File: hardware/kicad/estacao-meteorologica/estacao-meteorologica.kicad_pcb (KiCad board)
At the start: 2 copper layers, 109.4 x 61.3 mm, 126 parts, among them J101 Header, 1x02, P2.54 mm, J102 Header, 1x06, P2.54 mm, J103 Header, 1x03, P2.54 mm, J221 JST-XH, 1x04, P2.50 mm, J301 RJ11 6P6C, 90°, J501 RJ11 6P6C, 90°, J601 DC jack, 2.0 mm, J602 JST-XH, 1x02, P2.50 mm, J701 U.FL, 50 Ω, J801 microSD socket, TF-15x15, Q601 DMP6023LE-13, SW101 Tactile switch, SPST, U101 STM32F446RET6, U211 BMP280, U231 DHT22, U301 SN74LVC1G17DBVR, U401 SN74LVC1G17DBVR, U601 AP63205WU-7, U602 TLV62569DBVR, U701 LORA1276-C1-915MHZ, U801 SN74LVC125APWR, U802 EMIF06-MSD02N16, Y101 32.768 kHz, CL 7 pF, Y102 8 MHz, CL 10 pF

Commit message: Add test points necessarios para debug
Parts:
- added TP211: I2C1_SCL, TestPoint:TestPoint_Pad_D1.0mm, F.Cu at (126.2, 65.6)
- added TP212: I2C1_SDA, TestPoint:TestPoint_Pad_D1.0mm, F.Cu at (123.4, 65.4)
- added TP213: GND, TestPoint:TestPoint_Pad_D1.0mm, F.Cu at (127.5, 58.5)
- added TP221: BH_I2C3_SCL, TestPoint:TestPoint_Pad_D1.0mm, F.Cu at (115.9, 64.1)
- added TP222: BH_I2C3_SDA, TestPoint:TestPoint_Pad_D1.0mm, F.Cu at (118.7, 63.7)
- added TP223: GND, TestPoint:TestPoint_Pad_D1.0mm, F.Cu at (116.6, 60.0)
- added TP231: DHT22_DATA, TestPoint:TestPoint_Pad_D1.0mm, F.Cu at (126.4, 98.5)
- added TP232: GND, TestPoint:TestPoint_Pad_D1.0mm, F.Cu at (131.4, 107.1)
- TP301, TP302, TP303, TP401, TP402, TP403, TP501, TP502, TP503: footprint TestPoint:TestPoint_Pad_D1.5mm -> TestPoint:TestPoint_Pad_D1.0mm
- moved H902 69.9 mm to (137.0, 96.0)

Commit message: Refact: tirei estagio de 12V -> 5V e agora é direto 12V -> 3V
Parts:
- L601: value 4.7 µH -> 3.9 µH; footprint Inductor_SMD:L_Sunlord_MWSA0603S -> Inductor_SMD:L_APV_ANR5040
- U601: value AP63205WU-7 -> AP63203WU-7
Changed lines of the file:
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@@
 	(generator_version "9.0")
 	(general
-		(thickness 1.6)
+		(thickness 1.69)
 		(legacy_teardrops no)
 	)
@@
 	(layers
 		(0 "F.Cu" signal)
-		(2 "B.Cu" signal)
+		(2 "B.Cu" power)
 		(9 "F.Adhes" user "F.Adhesive")
 		(11 "B.Adhes" user "B.Adhesive")
@@
 	)
 	(setup
+		(stackup
+			(layer "F.SilkS"
+				(type "Top Silk Screen")
+			)
+			(layer "F.Paste"
+				(type "Top Solder Paste")
+			)
+			(layer "F.Mask"
+				(type "Top Solder Mask")
+				(thickness 0.01)
+			)
+			(layer "F.Cu"
+				(type "copper")
+				(thickness 0.035)
+			)
+			(layer "dielectric 1"
+				(type "core")
+				(thickness 1.6)
+				(material "FR4")
+				(epsilon_r 4.5)
+				(loss_tangent 0.02)
+			)
+			(layer "B.Cu"
+				(type "copper")
+				(thickness 0.035)
+			)
+			(layer "B.Mask"
+				(type "Bottom Solder Mask")
+				(thickness 0.01)
+			)
+			(layer "B.Paste"
+				(type "Bottom Solder Paste")
+			)
+			(layer "B.SilkS"
+				(type "Bottom Silk Screen")
+			)
+			(copper_finish "None")
+			(dielectric_constraints no)
+		)
 		(pad_to_mask_clearance 0)
 		(allow_soldermask_bridges_in_footprints no)
@@
 			)
 		)
-		(property "Value" "AP63205WU-7"
+		(property "Value" "AP63203WU-7"
 			(at 0 2.4 0)
 			(layer "F.Fab")
@@
 			)
 		)
-		(property "Datasheet" "https://www.lcsc.com/datasheet/lcsc_datasheet_2210280930_Diodes-Incorporated-AP63205WU-7_C2071056.pdf"
+		(property "Datasheet" "https://www.diodes.com/datasheet/download/AP63200-AP63201-AP63203-AP63205.pdf"
 			(at 0 0 0)
 			(layer "F.Fab")
@@
 			)
 		)
-		(property "Description" "-40℃~+85℃@(TA) 1 1.1MHz 22uA 2A 3.8V~32V 5V Buck Built-in Fixed Overcurrent Protection、Light load efficient mode、Cycle-by-cycle current limiting、Hiccup current limiting、EMI optimization (spread spectrum) Step-down type Yes TSOT-23-6 DC-DC Converters RoHS"
+		(property "Description" "Buck sincrono fixo 3,3V; VIN 3,8-32V; 2A; 1,1MHz; TSOT-23-6; protecao contra sobrecorrente e spread-spectrum EMI; RoHS"
 			(at 0 0 0)
 			(layer "F.Fab")
@@
 			)
 		)
-		(property "MPN" "AP63205WU-7"
+		(property "MPN" "AP63203WU-7"
 			(at 0 0 0)
 			(unlocked yes)
@@
 			)
 		)
-		(property "LCSC" "C2071056"
+		(property "LCSC" "C780769"
 			(at 0 0 0)
 			(unlocked yes)
@@
 			)
 		)
-		(property "LCSC Part" "C2071056"
+		(property "LCSC Part" "C780769"
 			(at 0 0 0)
 			(unlocked yes)
@@
 			)
 		)
-		(property "Rating" "5V fixos; 2A CI; VIN3.8-32V; 1.1MHz; IQtip22uA"
+		(property "Rating" "3,3V fixos; 2A CI; VIN3,8-32V; 1,1MHz; IQ tipico 22uA"
 			(at 0 0 0)
 			(unlocked yes)
@@
 			)
 		)
-		(property "Function" "Converte VIN_MAIN para5V; EN ligado aVIN; FB direto na saida filtrada"
+		(property "Function" "Converte VIN_MAIN diretamente para +3V3; EN ligado a VIN; FB direto na saida filtrada"
 			(at 0 0 0)
 			(unlocked yes)
@@
 			)
 		)
-		(property "Status_Ficha" "Conferido no catalogo em 2026-09-24; verificar estoque ao comprar"
+		(property "Status_Ficha" "Ficha do fabricante e catalogo LCSC conferidos em 2026-09-27; verificar estoque ao comprar"
 			(at 0 0 0)
 			(unlocked yes)
@@
 			)
 		)
-		(property "Specification" "5V fixos; 2A CI; VIN3.8-32V; 1.1MHz; IQtip22uA"
+		(property "Specification" "3,3V fixos; 2A CI; VIN3,8-32V; 1,1MHz; IQ tipico 22uA"
 			(at 0 0 0)
 			(unlocked yes)
@@
 			)
 		)
-		(property "Verification" "Conferido no catalogo em 2026-09-24; verificar estoque ao comprar"
+		(property "Verification" "Ficha do fabricante e catalogo LCSC conferidos em 2026-09-27; verificar estoque ao comprar"
 			(at 0 0 0)
 			(unlocked yes)
@@
 		)
 	)
-	(footprint "Inductor_SMD:L_Sunlord_MWSA0603S"
+	(footprint "Inductor_SMD:L_APV_ANR5040"
 		(layer "F.Cu")
 		(at 80.1 72.3)
-		(descr "Inductor, Sunlord, MWSA0603S, 7.0x6.6x2.8mm, (https://sunlordinc.com/Download.aspx?file=L1VwbG9hZEZpbGVzL1BERl9DYXQvMjAyMjExMTUxNDQ4MDU0NTQucGRm&lan=en), generated with kicad-footprint-generator gen_inductor.py")
-		(tags "mwsa")
+		(descr "Inductor, APV, ANR5040, 5.0x5.0x4.0mm, (http://en.apvind.com/public/upload/20240407/3375c395e460caa8519b4d637d9113ce.pdf), generated with kicad-footprint-generator gen_inductor.py")
+		(tags "wirewound power shielded")
 		(property "Reference" "L601"
-			(at 0 -4.25 0)
+			(at 0 -3.45 0)
 			(layer "F.SilkS")
 			(effects
@@
 			)
 		)
-		(property "Value" "4.7 µH"
-			(at 0 4.25 0)
+		(property "Value" "3.9 µH"
+			(at 0 3.45 0)
 			(layer "F.Fab")
 			(effects
@@
 			)
 		)
-		(property "Datasheet" "https://www.lcsc.com/datasheet/lcsc_datasheet_2310251550_Sunlord-MWSA0603S-4R7MT_C408447.pdf"
+		(property "Datasheet" "https://www.lcsc.com/product-detail/Power-Inductors_APV-ANR5040T3R9M_C7427132.html"
 			(at 0 0 0)
 			(layer "F.Fab")
@@
 			)
 		)
-		(property "Description" "33mΩ 4.7uH 6A 9A ±20% SMD,7x6.6mm Power Inductors RoHS"
+		(property "Description" "Indutor de potencia blindado 3,9uH ±20%; Irms 3,7A; Isat 4,2A; SMD 5x5mm; RoHS"
 			(at 0 0 0)
 			(layer "F.Fab")
@@
 			)
 		)
-		(property "Manufacturer" "Sunlord"
+		(property "Manufacturer" "APV"
 			(at 0 0 0)
 			(unlocked yes)
@@
 			)
 		)
-		(property "MPN" "MWSA0603S-4R7MT"
+		(property "MPN" "ANR5040T3R9M"
 			(at 0 0 0)
 			(unlocked yes)
@@
 			)
 		)
-		(property "LCSC" "C408447"
+		(property "LCSC" "C7427132"
 			(at 0 0 0)
 			(unlocked yes)
@@
 			)
 		)
-		(property "LCSC Part" "C408447"
+		(property "LCSC Part" "C7427132"
 			(at 0 0 0)
 			(unlocked yes)
@@
 			)
 		)
-		(property "Rating" "Isat min7.2A/tip9A; Irms min5A; DCRmax33mOhm"
+		(property "Rating" "L=3,9uH ±20%; Irms 3,7A; Isat 4,2A; indutor blindado; corpo 5x5x4mm"
 			(at 0 0 0)
 			(unlocked yes)
@@
 			)
 		)
-		(property "Modelo 3D" "${KICAD9_3DMODEL_DIR}/Inductor_SMD.3dshapes/L_Sunlord_MWSA0603S.step"
+		(property "Modelo 3D" "${KICAD9_3DMODEL_DIR}/Inductor_SMD.3dshapes/L_APV_ANR5040.step"
 			(at 0 0 0)
 			(unlocked yes)
@@
 			)
 		)
-		(property "Status_Ficha" "Conferido no catalogo em 2026-09-24; verificar estoque ao comprar"
+		(property "Status_Ficha" "Ficha do fabricante e catalogo LCSC conferidos em 2026-09-27; verificar estoque ao comprar"
 			(at 0 0 0)
 			(unlocked yes)
@@
 			)
 		)
-		(property "Specification" "Isat min7.2A/tip9A; Irms min5A; DCRmax33mOhm"
+		(property "Specification" "L=3,9uH ±20%; Irms 3,7A; Isat 4,2A; indutor blindado; corpo 5x5x4mm"
 			(at 0 0 0)
 			(unlocked yes)
@@
 			)
 		)
-		(property "Verification" "Conferido no catalogo em 2026-09-24; verificar estoque ao comprar"
+		(property "Verification" "Ficha do fabricante e catalogo LCSC conferidos em 2026-09-27; verificar estoque ao comprar"
 			(at 0 0 0)
 			(unlocked yes)
@@
 		(attr smd)
 		(fp_line
-			(start -3.61 -3.41)
-			(end 3.61 -3.41)
+			(start -2.61 -2.61)
+			(end 2.61 -2.61)
 			(stroke
 				(width 0.12)
@@
 		)
 		(fp_line
-			(start -3.61 -2.01)
-			(end -3.61 -3.41)
+			(start -2.61 -2.36)
+			(end -2.61 -2.61)
 			(stroke
 				(width 0.12)
@@
 		)
 		(fp_line
-			(start -3.61 3.41)
-			(end -3.61 2.01)
+			(start -2.61 2.61)
+			(end -2.61 2.36)
 			(stroke
 				(width 0.12)
@@
 		)
 		(fp_line
-			(start 3.61 -3.41)
-			(end 3.61 -2.01)
+			(start 2.61 -2.61)
+			(end 2.61 -2.36)
 			(stroke
 				(width 0.12)
@@
 		)
 		(fp_line
-			(start 3.61 2.01)
-			(end 3.61 3.41)
+			(start 2.61 2.36)
+			(end 2.61 2.61)
 			(stroke
 				(width 0.12)
@@
 		)
 		(fp_line
-			(start 3.61 3.41)
-			(end -3.61 3.41)
+			(start 2.61 2.61)
+			(end -2.61 2.61)
 			(stroke
 				(width 0.12)
@@
 		)
 		(fp_line
-			(start -4.45 -2)
-			(end -3.75 -2)
+			(start -2.8 -2.35)
+			(end -2.75 -2.35)
 			(stroke
 				(width 0.05)
@@
 		)
 		(fp_line
-			(start -4.45 2)
-			(end -4.45 -2)
+			(start -2.8 2.35)
+			(end -2.8 -2.35)
 			(stroke
 				(width 0.05)
@@
 		)
 		(fp_line
-			(start -3.75 -3.55)
-			(end 3.75 -3.55)
+			(start -2.75 -2.75)
+			(end 2.75 -2.75)
 			(stroke
 				(width 0.05)
@@
 		)
 		(fp_line
-			(start -3.75 -2)
-			(end -3.75 -3.55)
+			(start -2.75 -2.35)
+			(end -2.75 -2.75)
 			(stroke
 				(width 0.05)
@@
 		)
 		(fp_line
-			(start -3.75 2)
-			(end -4.45 2)
+			(start -2.75 2.35)
+			(end -2.8 2.35)
 			(stroke
 				(width 0.05)
@@
 		)
 		(fp_line
-			(start -3.75 3.55)
-			(end -3.75 2)
+			(start -2.75 2.75)
+			(end -2.75 2.35)
 			(stroke
 				(width 0.05)
@@
 		)
 		(fp_line
-			(start 3.75 -3.55)
-			(end 3.75 -2)
+			(start 2.75 -2.75)
+			(end 2.75 -2.35)
 			(stroke
 				(width 0.05)
@@
 		)
 		(fp_line
-			(start 3.75 -2)
-			(end 4.45 -2)
+			(start 2.75 -2.35)
+			(end 2.8 -2.35)
 			(stroke
 				(width 0.05)
@@
 		)
 		(fp_line
-			(start 3.75 2)
-			(end 3.75 3.55)
+			(start 2.75 2.35)
+			(end 2.75 2.75)
 			(stroke
 				(width 0.05)
@@
 		)
 		(fp_line
-			(start 3.75 3.55)
-			(end -3.75 3.55)
+			(start 2.75 2.75)
+			(end -2.75 2.75)
 			(stroke
 				(width 0.05)
@@
 		)
 		(fp_line
-			(start 4.45 -2)
-			(end 4.45 2)
+			(start 2.8 -2.35)
+			(end 2.8 2.35)
 			(stroke
 				(width 0.05)
@@
 		)
 		(fp_line
-			(start 4.45 2)
-			(end 3.75 2)
+			(start 2.8 2.35)
+			(end 2.75 2.35)
 			(stroke
 				(width 0.05)
@@
 		)
 		(fp_rect
-			(start -3.5 -3.3)
-			(end 3.5 3.3)
+			(start -2.5 -2.5)
+			(end 2.5 2.5)
 			(stroke
 				(width 0.1)
@@
 		)
 		(pad "1" smd roundrect
-			(at -3.025 0)
-			(size 2.35 3.5)
+			(at -1.85 0)
+			(size 1.4 4.2)
 			(layers "F.Cu" "F.Mask" "F.Paste")
-			(roundrect_rratio 0.106383)
+			(roundrect_rratio 0.178571)
 			(net 7 "Net-(U601-SW)")
 			(pinfunction "1")
@@
 		)
 		(pad "2" smd roundrect
-			(at 3.025 0)
-			(size 2.35 3.5)
+			(at 1.85 0)
+			(size 1.4 4.2)
 			(layers "F.Cu" "F.Mask" "F.Paste")
-			(roundrect_rratio 0.106383)
+			(roundrect_rratio 0.178571)
 			(net 9 "+5V")
 			(pinfunction "2")
@@
 		)
 		(embedded_fonts no)
-		(model "${KICAD9_3DMODEL_DIR}/Inductor_SMD.3dshapes/L_Sunlord_MWSA0603S.step"
+		(model "${KICAD9_3DMODEL_DIR}/Inductor_SMD.3dshapes/L_APV_ANR5040.step"
 			(offset
 				(xyz 0 0 0)

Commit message: rotemento 3.0
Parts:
- removed C608: 4.7 µF, 25 V, Capacitor_SMD:C_0805_2012Metric
- removed C609, C610, C611: 10 µF, 6.3 V, Capacitor_SMD:C_0402_1005Metric
- removed L602: 2.2 µH, Hardware_Power:L_Abracon_ASPI-0530HI
- removed R602: 453 kΩ, 1 %, Resistor_SMD:R_0603_1608Metric
- removed R603: 100 kΩ, 1 %, Resistor_SMD:R_0402_1005Metric
- removed TP602: +5V, TestPoint:TestPoint_Pad_D1.5mm
- removed U602: TLV62569DBVR, Package_TO_SOT_SMD:SOT-23-5
- J801: footprint Hardware_SD_Interface:microSD_SOFNG_TF-15x15 -> Hardware_SD_Interface:microSD_SOFNG_TF-15x15_C111196
- moved H902 97.0 mm to (43.1, 120.3)
- moved C105 33.3 mm to (118.6, 89.3)
- moved D221 29.7 mm to (139.1, 63.2)
- moved D222 29.7 mm to (142.8, 63.2)
- moved J221 29.7 mm to (133.3, 58.6)
- moved TP222 26.5 mm to (145.2, 63.2)
- moved TP604 16.6 mm to (75.9, 81.8)
- moved C113 16.0 mm to (102.5, 87.7), turned to -90 degrees
- moved TP603 15.1 mm to (85.4, 72.0)
- moved TP601 14.4 mm to (70.8, 70.5)
- moved TP223 12.1 mm to (128.4, 57.4)
- moved TP213 9.91 mm to (122.4, 67.0)
- moved TP211 6.90 mm to (119.3, 65.8)
- moved TP212 5.66 mm to (118.1, 63.4)
- moved J101 5.14 mm to (106.4, 65.2), turned to 90 degrees
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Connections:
- net BH_I2C3_SCL renamed /BH1750_INTERFACE/BH_I2C3_SCL
- net Net-(U601-SW) renamed /ALIMENTAÇÃO/V_SW
- C606 pad 1: +5V -> +3V3
- C607 pad 1: +5V -> +3V3
- D222 pad 2: BH_I2C3_SDA -> /BH1750_INTERFACE/BH_I2C3_SDA
- J221 pad 2: +3V3 -> /BH1750_INTERFACE/BH_I2C3_SDA
- J221 pad 4: BH_I2C3_SDA -> unconnected-(J221-Pin_4-Pad4)
- L601 pad 2: +5V -> +3V3
- R106 pad 2: BH_I2C3_SDA -> /BH1750_INTERFACE/BH_I2C3_SDA
- TP222 pad 1: BH_I2C3_SDA -> /BH1750_INTERFACE/BH_I2C3_SDA
- U101 pad 40: BH_I2C3_SDA -> /BH1750_INTERFACE/BH_I2C3_SDA
- U601 pad 1: +5V -> +3V3
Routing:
- net +3V3: track 0.00 -> 143.6 mm, vias 0 -> 4
- net GND: track 0.00 -> 90.5 mm, vias 0 -> 43
- net /INTERFACES METEOROLÓGICAS/WIND_SPEED_PULSE: track 0.00 -> 63.5 mm, vias 0 -> 4
- net /INTERFACES METEOROLÓGICAS/WIND_DIR_ADC: track 0.00 -> 61.7 mm, vias 0 -> 2
- net /INTERFACES METEOROLÓGICAS/RAIN_PULSE: track 0.00 -> 45.7 mm
- net VBAT: track 0.00 -> 42.4 mm, vias 0 -> 2
- net /MCU E DEPURAÇÃO/DHT22_DATA: track 0.00 -> 38.7 mm, vias 0 -> 2
- net /RÁDIO LoRa/+3V3_LORA: track 0.00 -> 37.8 mm
- net /BH1750_INTERFACE/BH_I2C3_SCL: track 0.00 -> 33.5 mm
- net /ALIMENTAÇÃO/VIN_MAIN: track 0.00 -> 28.1 mm
- net /MCU E DEPURAÇÃO/LORA_SPI_SCK: track 0.00 -> 26.0 mm
- net /MCU E DEPURAÇÃO/LORA_DIO2: track 0.00 -> 19.4 mm, vias 0 -> 2
- net /MCU E DEPURAÇÃO/I2C1_SDA: track 0.00 -> 18.2 mm
- net Net-(D601-A2): track 0.00 -> 18.1 mm
- net /MCU E DEPURAÇÃO/LORA_SPI_MOSI: track 0.00 -> 17.6 mm
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- added copper zone on F.Cu, net +3V3
- added copper zone on F.Cu, net /ALIMENTAÇÃO/VIN_MAIN
- added copper zone on F.Cu, net /ALIMENTAÇÃO/V_SW
- added copper zone on B.Cu, net GND
- added copper zone on F.Cu, net GND

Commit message: feat(hardware): consolida revisão PCB V2
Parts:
- TP304, TP404, TP504, TP601, TP603, TP604: footprint TestPoint:TestPoint_Pad_D1.5mm -> TestPoint:TestPoint_Pad_D1.0mm
- moved J102 48.8 mm to (113.2, 57.8)
- moved BT101 37.1 mm to (83.6, 60.4), turned to 180 degrees
- moved SW101 28.1 mm to (108.3, 97.4), turned to 0 degrees
- moved C113 26.5 mm to (97.5, 61.7)
- moved TP213 26.3 mm to (97.5, 58.4)
- moved TP222 25.2 mm to (120.0, 63.5)
- moved R801 21.2 mm to (95.3, 93.0)
- moved U801 21.2 mm to (91.6, 90.4)
- moved C802 21.2 mm to (94.0, 95.5)
- moved D222 21.1 mm to (121.8, 62.2)
- moved C114 20.7 mm to (102.8, 97.4), turned to -90 degrees
- moved J801 19.6 mm to (79.1, 95.9)
- moved R102 18.8 mm to (101.0, 97.4)
- moved R802 18.2 mm to (71.9, 88.8)
- moved C801 18.1 mm to (68.7, 93.7)
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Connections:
- D221 pad 2: /BH1750_INTERFACE/BH_I2C3_SCL -> /BH1750_INTERFACE/BH_I2C3_SDA
- D222 pad 2: /BH1750_INTERFACE/BH_I2C3_SDA -> /BH1750_INTERFACE/BH_I2C3_SCL
- J102 pad 2: GND -> SWDIO
- J102 pad 3: SWDIO -> SWCLK
- J102 pad 4: SWCLK -> SWO
- J102 pad 6: SWO -> GND
- J221 pad 2: /BH1750_INTERFACE/BH_I2C3_SDA -> /BH1750_INTERFACE/BH_I2C3_SCL
- J221 pad 3: /BH1750_INTERFACE/BH_I2C3_SCL -> /BH1750_INTERFACE/BH_I2C3_SDA
- J221 pad 4: unconnected-(J221-Pin_4-Pad4) -> +3V3
- R801 pad 1: /CARTÃO microSD/SD_SPI_CS -> /CARTÃO microSD/SD_SPI_MOSI
- TP221 pad 1: /BH1750_INTERFACE/BH_I2C3_SCL -> /BH1750_INTERFACE/BH_I2C3_SDA
- TP222 pad 1: /BH1750_INTERFACE/BH_I2C3_SDA -> /BH1750_INTERFACE/BH_I2C3_SCL
- U801 pad 11: SD_CS_BUF -> SD_MOSI_BUF
- U801 pad 12: /CARTÃO microSD/SD_SPI_CS -> /CARTÃO microSD/SD_SPI_MOSI
- U801 pad 2: /CARTÃO microSD/SD_SPI_MOSI -> SD_MISO_BUF
- U801 pad 3: SD_MOSI_BUF -> /CARTÃO microSD/SD_MISO
- U801 pad 5: SD_MISO_BUF -> /CARTÃO microSD/SD_SCK
- U801 pad 6: /CARTÃO microSD/SD_MISO -> SD_SCK_BUF
- U801 pad 8: SD_SCK_BUF -> SD_CS_BUF
- U801 pad 9: /CARTÃO microSD/SD_SCK -> /CARTÃO microSD/SD_SPI_CS
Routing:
- net +3V3: track 143.6 -> 404.9 mm, vias 4 -> 5
- net AVREF_SENSOR: track 6.06 -> 53.3 mm, vias 0 -> 2
- net NRST: track 11.4 -> 56.1 mm, vias 0 -> 3
- net GND: track 90.5 -> 121.3 mm, vias 43 -> 95
- net /MCU E DEPURAÇÃO/LORA_RST: track 16.1 -> 42.4 mm, vias 0 -> 2
- net SWDIO: track 0.00 -> 23.9 mm, vias 0 -> 1
- net VBAT: track 42.4 -> 20.8 mm
- net /BH1750_INTERFACE/BH_I2C3_SDA: track 17.0 -> 37.9 mm, vias 0 -> 4
- net /CARTÃO microSD/SD_SPI_CS: track 0.00 -> 20.7 mm
- net /MCU E DEPURAÇÃO/LORA_NSS: track 12.0 -> 31.9 mm, vias 0 -> 2
- net SWO: track 0.00 -> 19.2 mm, vias 0 -> 1
- net SWCLK: track 0.00 -> 19.0 mm, vias 0 -> 1
- net /CARTÃO microSD/SD_SPI_MOSI: track 0.00 -> 14.6 mm
- net /CARTÃO microSD/SD_SCK: track 0.00 -> 14.1 mm
- net SD_CARD_DAT1: track 0.00 -> 13.8 mm
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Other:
- board size 109.4 x 61.3 mm -> 96.9 x 56.3 mm

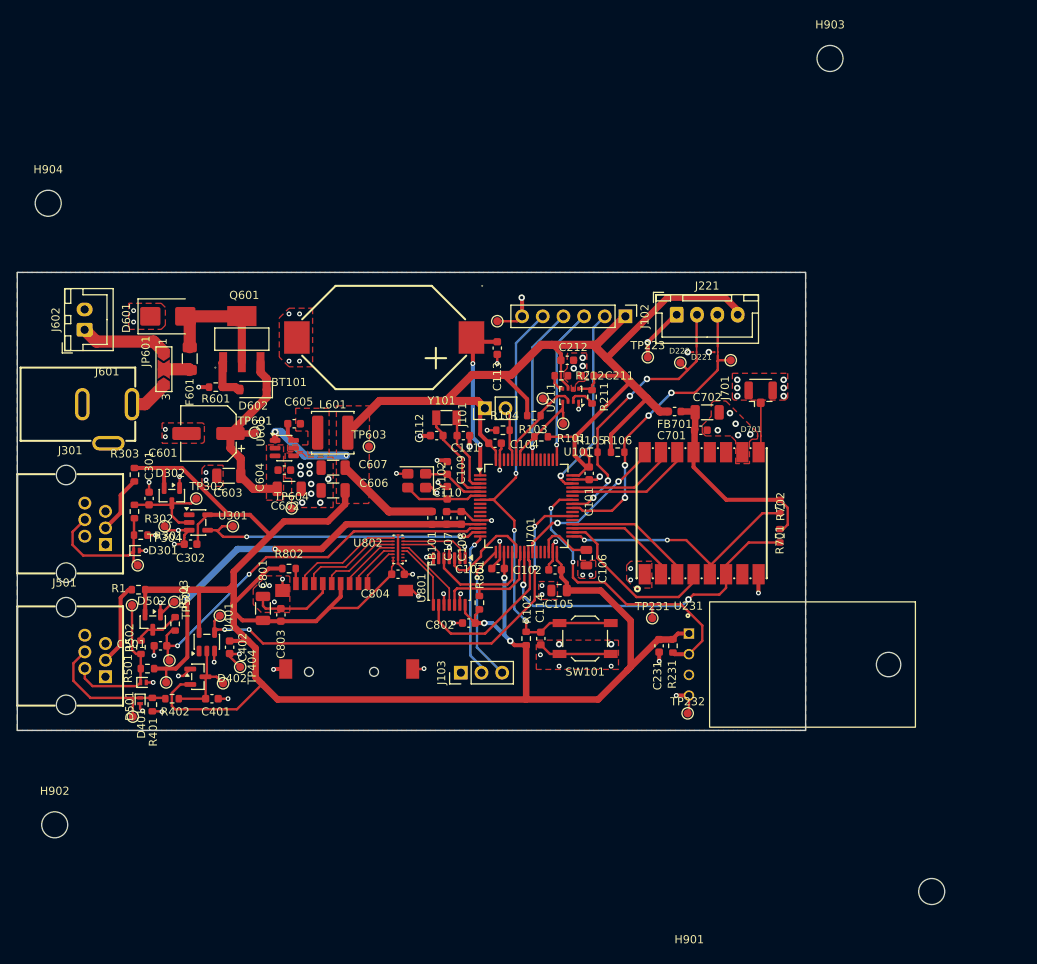
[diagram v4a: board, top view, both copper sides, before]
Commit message: Finalizado layout PCBV2
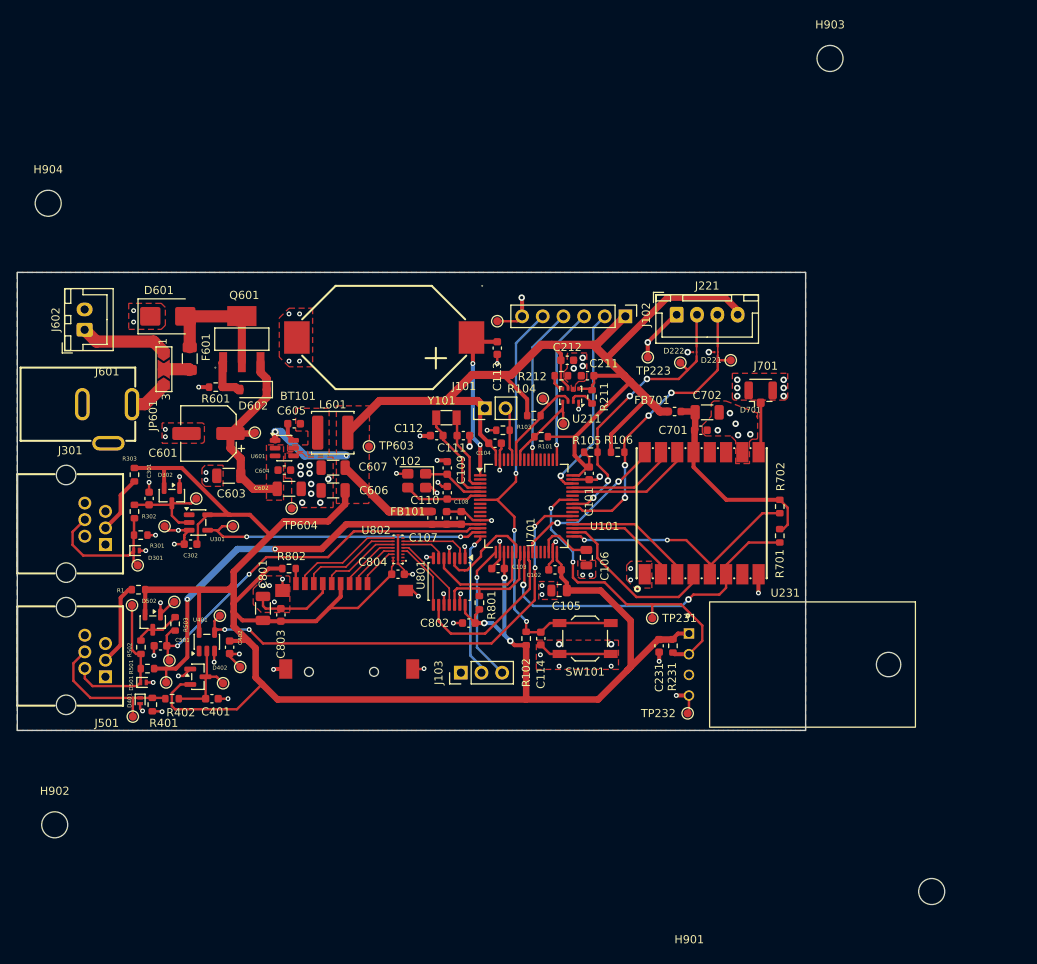
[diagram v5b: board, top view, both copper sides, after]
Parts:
- moved D701 2.40 mm to (129.6, 70.1)
